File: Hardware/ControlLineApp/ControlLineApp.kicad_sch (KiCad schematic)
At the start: 10 parts, among them J2 Conn_02x09

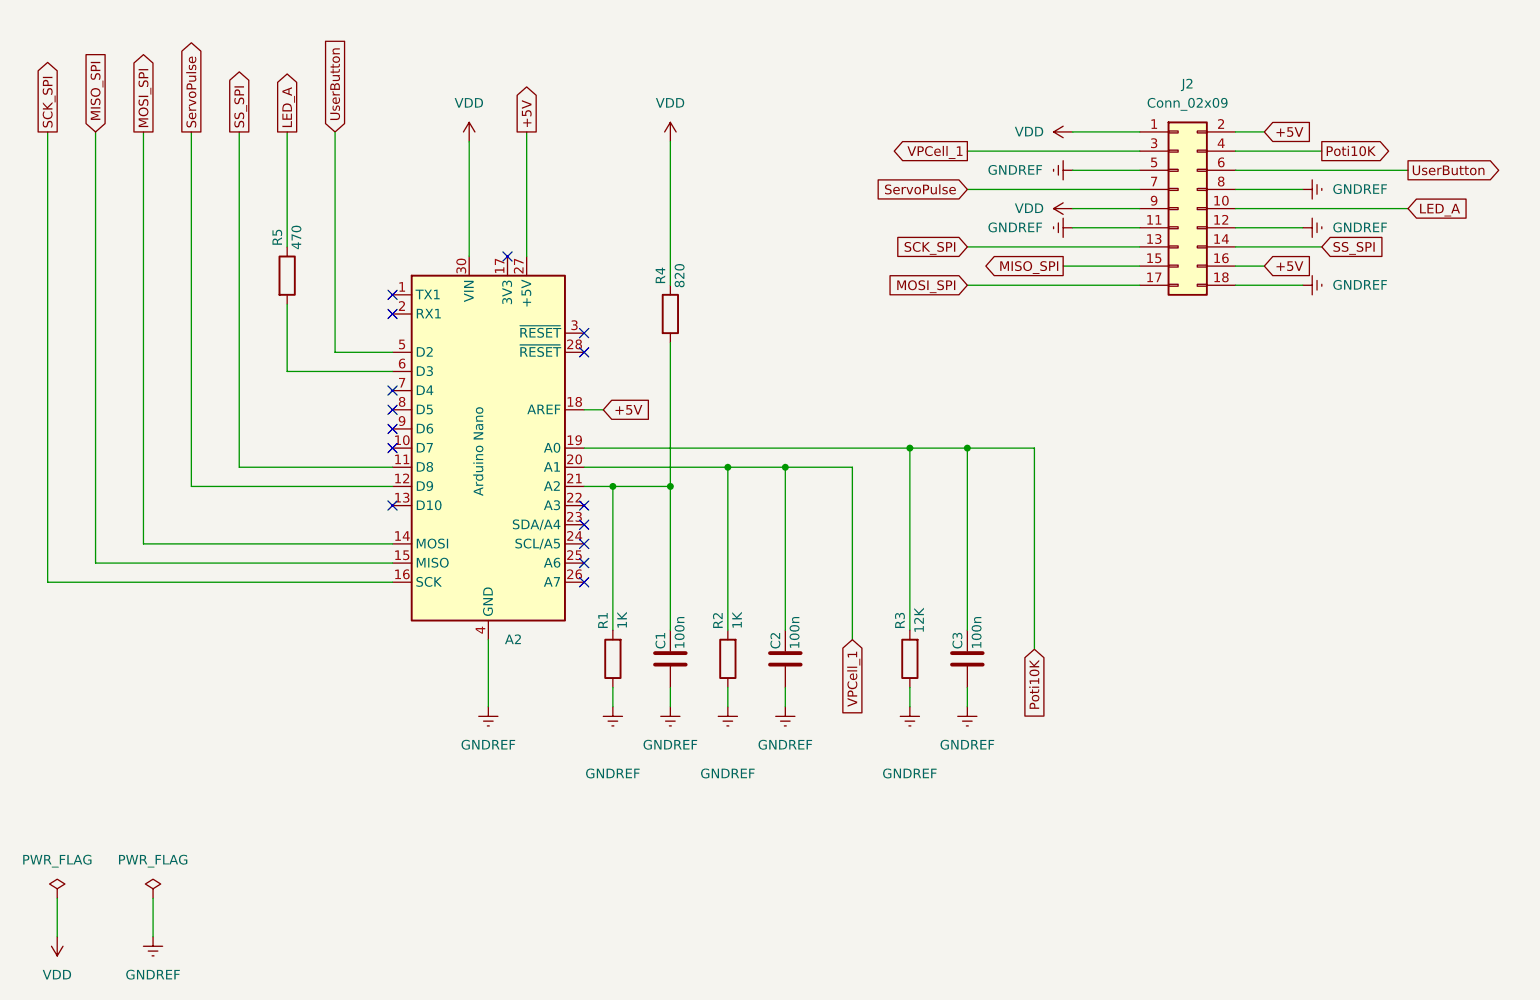
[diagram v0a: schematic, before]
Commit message: PCB and schematic adapted with I²C interface, software implementation accelerometer gyroscope
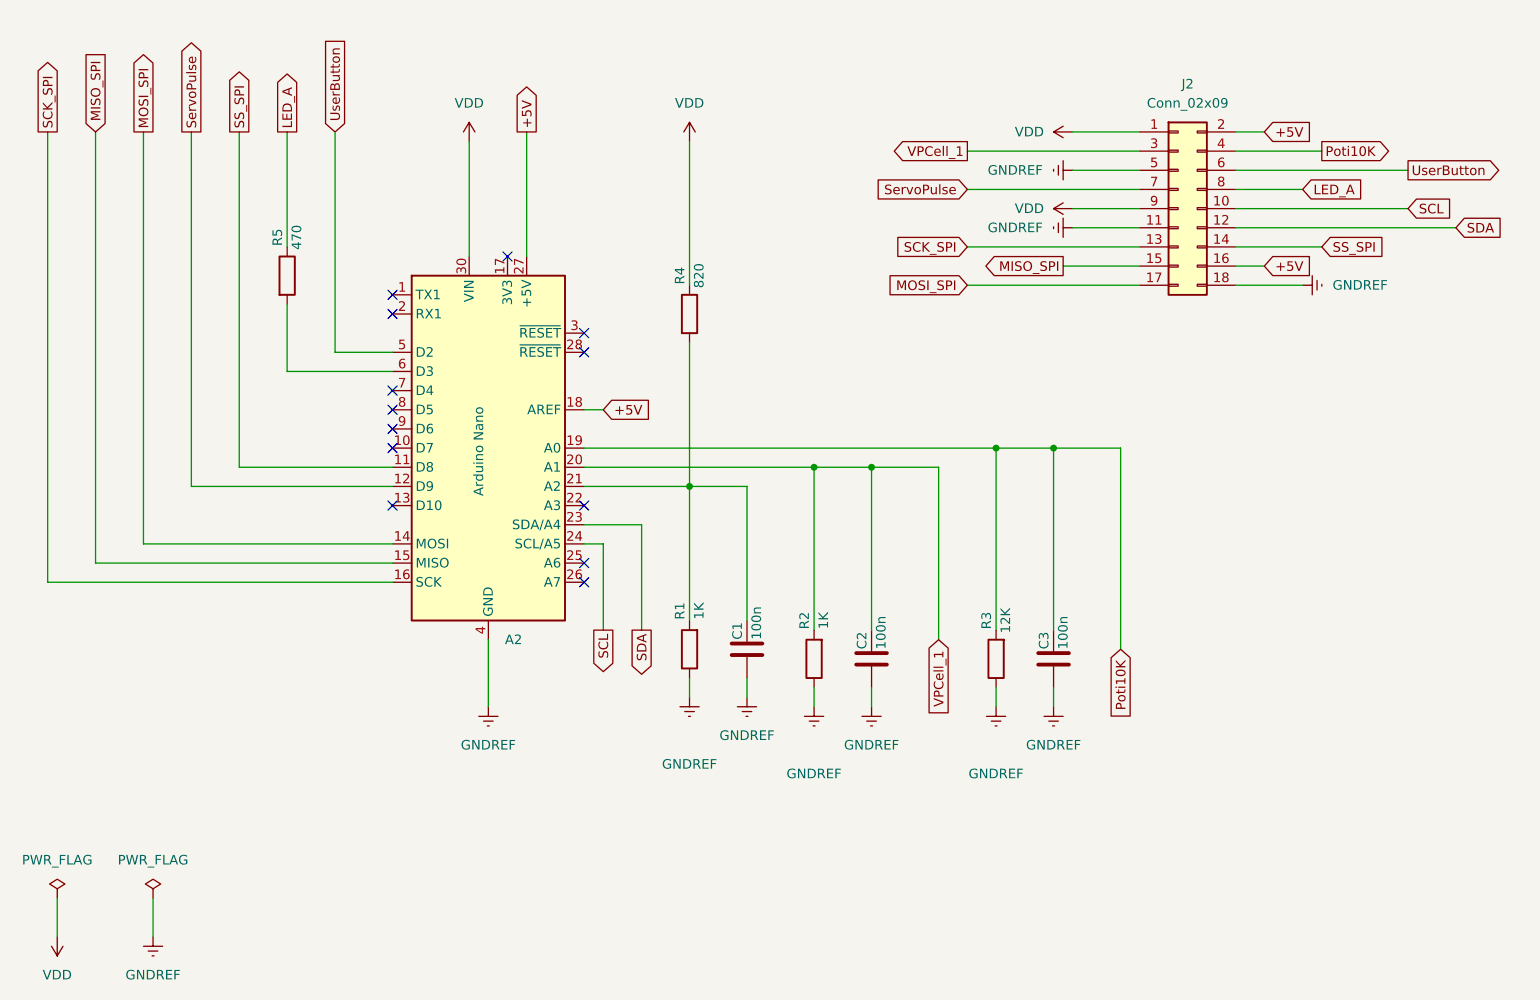
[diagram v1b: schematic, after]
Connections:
- net GNDREF: no longer J2.12 (Pin_12), J2.8 (Pin_8)
- net LED_A: now also J2.8 (Pin_8); no longer J2.10 (Pin_10)
- net SDA: now reaches A2.23 (SDA/A4)
- net SDA: now also J2.12 (Pin_12)
- net SCL: now reaches A2.24 (SCL/A5)
- net SCL: now also J2.10 (Pin_10)
- no-connect marks 15 -> 13
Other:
- moved on the sheet: C1, C2, C3, R1, R2, R3, R4
